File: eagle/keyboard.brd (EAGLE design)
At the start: 100 x 100 mm, 72 parts, among them IC1 STC12C5616AD, J4 RESERVED, Q1 12MHz

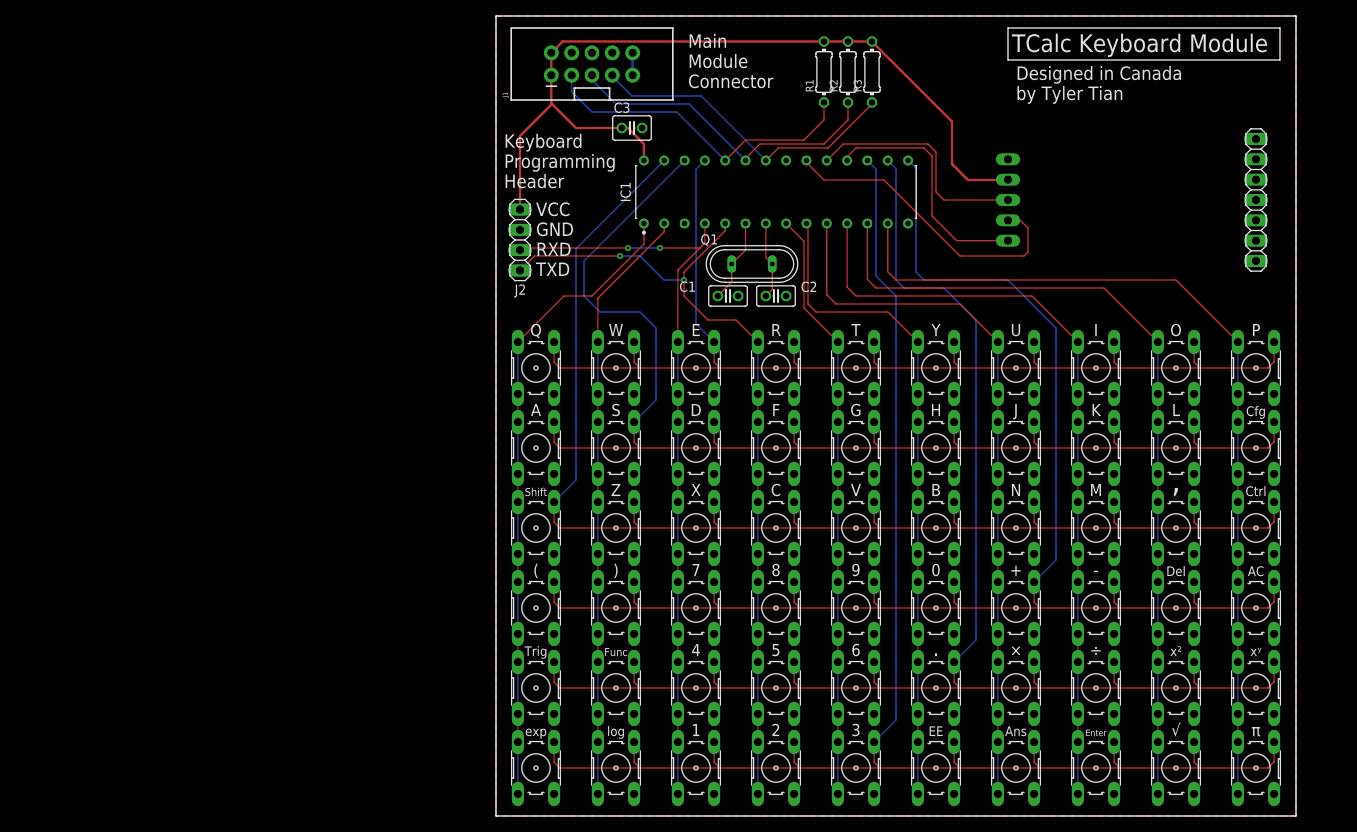
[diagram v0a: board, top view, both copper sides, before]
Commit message: Add reset button to keyboard module
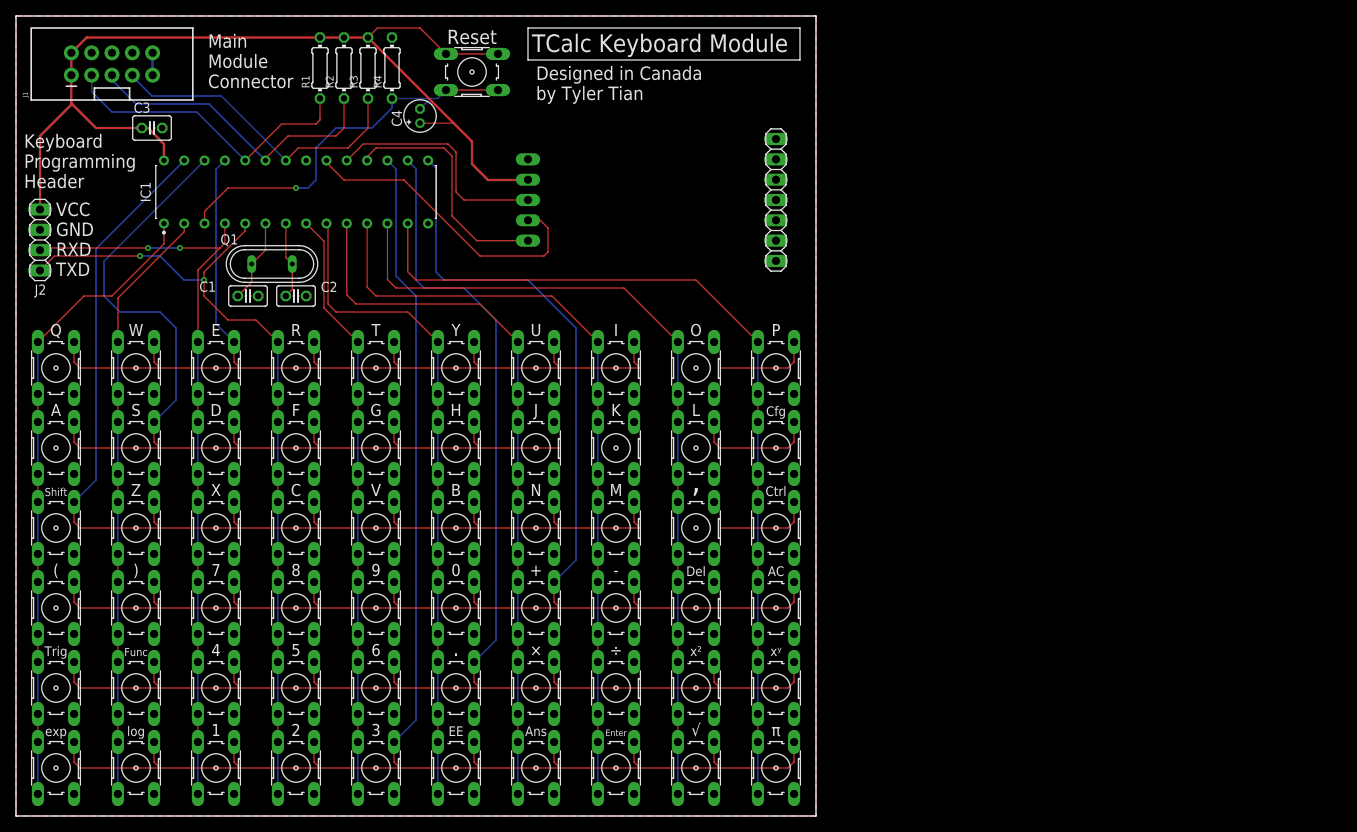
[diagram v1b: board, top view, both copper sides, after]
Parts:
- added C4: 10uF, rcl:E1,8-4
- added R4: 10K, rcl:0204/7
- added S61: (no value), switch-omron:B3F-10XX
- moved R1 63.0 mm to (38.0, 93.5)
- moved R2 63.0 mm to (41.0, 93.5)
- moved R3 63.0 mm to (44.0, 93.5)
- moved C1 60.0 mm to (29.0, 65.0)
- moved C2 60.0 mm to (35.0, 65.0)
- moved C3 60.0 mm to (17.0, 86.0)
- moved IC1 60.0 mm to (35.0, 78.0)
- moved J1 60.0 mm to (12.0, 94.0)
- moved J2 60.0 mm to (3.00, 72.0)
- moved J3 60.0 mm to (64.0, 77.0)
- moved J4 60.0 mm to (95.0, 77.0)
- moved Q1 60.0 mm to (32.0, 69.0)
- moved S1 60.0 mm to (5.00, 56.0)
- moved S10 60.0 mm to (95.0, 56.0)
- moved S11 60.0 mm to (5.00, 46.0)
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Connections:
- new net N$2: C4.-, IC1.3, R4.1, S61.3, S61.4
- net GND: now also R4.2
- net VCC: now also C4.+, S61.1, S61.2
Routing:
- net N$2: track 0.00 -> 49.4 mm, vias 0 -> 1
- net ROW2: track 169.8 -> 142.7 mm
- net VCC: track 104.9 -> 126.1 mm
- net ROW3: track 172.5 -> 158.9 mm
- net ROW1: track 148.2 -> 134.6 mm
- net ROW5: track 195.4 -> 191.8 mm
- net ROW4: track 191.7 -> 188.2 mm
- net SBDI_EN: track 41.5 -> 39.0 mm
- net SBDI_CLK: track 41.2 -> 39.3 mm
- net SBDI_DAT: track 40.1 -> 39.3 mm
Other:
- board text added: "Reset"
